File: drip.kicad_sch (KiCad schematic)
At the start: 37 parts, among them J1 ISP, Q1 2n2907, Q2 2n2907, Q3 2n2907, Q4 2n2907, Q5 2n2907, Q6 2n2907, Q7 2n2907, Q8 2n2907, SW1 8, SW10 Divide, SW11 Divide, SW12 Divide, SW2 5, SW3 2, SW4 Decimal, SW5 9, SW6 6, SW7 3, SW8 CHS, SW9 Divide, U1 74LS138, U2 5641AS-4Digit-7Segment, U3 5641AS-4Digit-7Segment, U4 MSP430G2553IN20

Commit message: Reducing pins
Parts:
- removed SW1: 8, Button_Switch_Keyboard:SW_Cherry_MX_1.00u_PCB, symbol Switch:SW_Push_45deg
- removed SW10, SW11, SW12, SW9: Divide, Button_Switch_Keyboard:SW_Cherry_MX_1.00u_PCB, symbol Switch:SW_Push_45deg
- removed SW2: 5, Button_Switch_Keyboard:SW_Cherry_MX_1.00u_PCB, symbol Switch:SW_Push_45deg
- removed SW3: 2, Button_Switch_Keyboard:SW_Cherry_MX_1.00u_PCB, symbol Switch:SW_Push_45deg
- removed SW4: Decimal, Button_Switch_Keyboard:SW_Cherry_MX_1.00u_PCB, symbol Switch:SW_Push_45deg
- removed SW5: 9, Button_Switch_Keyboard:SW_Cherry_MX_1.00u_PCB, symbol Switch:SW_Push_45deg
- removed SW6: 6, Button_Switch_Keyboard:SW_Cherry_MX_1.00u_PCB, symbol Switch:SW_Push_45deg
- removed SW7: 3, Button_Switch_Keyboard:SW_Cherry_MX_1.00u_PCB, symbol Switch:SW_Push_45deg
- removed SW8: CHS, Button_Switch_Keyboard:SW_Cherry_MX_1.00u_PCB, symbol Switch:SW_Push_45deg
- added JP? (x2): Jumper_2_Bridged, symbol Jumper:Jumper_2_Bridged
- added R? (x8): R_Small_US, symbol Device:R_Small_US
- added SW?: And, symbol Switch:SW_Push_45deg
- added SW?: 8, symbol Switch:SW_Push_45deg
- added SW?: 9, symbol Switch:SW_Push_45deg
- added SW?: Xor, symbol Switch:SW_Push_45deg
- added SW?: 2, symbol Switch:SW_Push_45deg
- added SW?: E, symbol Switch:SW_Push_45deg
- added SW?: Decimal, symbol Switch:SW_Push_45deg
- added SW?: Clear, symbol Switch:SW_Push_45deg
- added SW?: F, symbol Switch:SW_Push_45deg
- added SW?: 5, symbol Switch:SW_Push_45deg
- added SW?: A, symbol Switch:SW_Push_45deg
- added SW?: 1, symbol Switch:SW_Push_45deg
- added SW?: Shift, symbol Switch:SW_Push_45deg
- added SW?: 0, symbol Switch:SW_Push_45deg
- added SW?: K, symbol Switch:SW_Push_45deg
- added SW?: Dec, symbol Switch:SW_Push_45deg
- added SW?: Enter, symbol Switch:SW_Push_45deg
- added SW?: D, symbol Switch:SW_Push_45deg
- added SW?: 7, symbol Switch:SW_Push_45deg
- added SW?: Oct, symbol Switch:SW_Push_45deg
- added SW?: Mul, symbol Switch:SW_Push_45deg
- added SW?: Plus, symbol Switch:SW_Push_45deg
- added SW?: +/-, symbol Switch:SW_Push_45deg
- added SW?: Minus, symbol Switch:SW_Push_45deg
- added SW?: Or, symbol Switch:SW_Push_45deg
- added SW?: 3, symbol Switch:SW_Push_45deg
- added SW?: B, symbol Switch:SW_Push_45deg
- added SW?: Hex, symbol Switch:SW_Push_45deg
- added SW?: 1'sCompl, symbol Switch:SW_Push_45deg
- added SW?: 6, symbol Switch:SW_Push_45deg
- added SW?: Clear Entry, symbol Switch:SW_Push_45deg
- added SW?: Div, symbol Switch:SW_Push_45deg
- added SW?: Bin, symbol Switch:SW_Push_45deg
- added SW?: 4, symbol Switch:SW_Push_45deg
- added SW?: Store, symbol Switch:SW_Push_45deg
- added SW?: C, symbol Switch:SW_Push_45deg
- added SW?: Recall, symbol Switch:SW_Push_45deg
- added U?: 74LS595, Package_DIP:DIP-16_W7.62mm_Socket_LongPads, symbol 74xx:74LS595
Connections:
- net GND: now also JP?.1 (A), JP?.1 (A), U?.8 (GND)
- net VCC: now also U?.10 (~{SRCLR}), U?.16 (VCC)
- net ~{LED_SEL_0}: now also U4.2 (TA0CLK/ACLK/CA0/A0/P1.0)
- net ~{LED_SEL_1}: now also U4.3 (UCA0RXD/UCA0SOMI/TA0.0/CA1/A1/P1.1)
- net ~{LED_SEL_2}: now also U4.4 (UCA0TXD/UCA0SIMO/TA0.1/CA2/A2/P1.2)
- net d0: no longer names the net of U2.11 (A), U3.11 (A)
- net d0: now also R?.2; no longer U4.2 (TA0CLK/ACLK/CA0/A0/P1.0)
- net d1: no longer names the net of U2.7 (B), U3.7 (B)
- net d1: now also R?.2; no longer U4.3 (UCA0RXD/UCA0SOMI/TA0.0/CA1/A1/P1.1)
- net d2: no longer names the net of U2.4 (C), U3.4 (C)
- net d2: now also R?.2; no longer U4.4 (UCA0TXD/UCA0SIMO/TA0.1/CA2/A2/P1.2)
- net d3: no longer names the net of U2.2 (D), U3.2 (D)
- net d3: now also R?.2; no longer U4.5 (CAOUT/VREF-/VeREF-/CA3/A3/P1.3)
- net d4: no longer names the net of U2.1 (E), U3.1 (E)
- net d4: now also R?.2; no longer U4.6 (TCK/SMCLK/UCB0STE/UCA0CLK/VREF+/VeREF+/CA4/A4/P1.4)
- net d5: no longer names the net of U2.10 (F), U3.10 (F)
- net d5: now also R?.2; no longer U4.7 (TMS/UCB0CLK/UCA0STE/TA0.0/CA5/A5/P1.5)
- net d6: no longer names the net of U2.5 (G), U3.5 (G)
- net d6: now also R?.2; no longer U4.14 (TDI/TCLK/UCB0SOMI/UCB0SCL/TA0.1/CA6/A6/P1.6)
- net d7: no longer names the net of U2.3 (DP), U3.3 (DP)
- net d7: now also R?.2; no longer U4.15 (TDO/TDI/UCB0SIMO/UCB0SDA/CAOUT/CA7/A7/P1.7)
- new net: JP?.2 (B), U?.13 (~{OE})
- new net: JP?.2 (B), U?.12 (RCLK)
- new net LED_A: R?.1, U?.15 (QA)
- new net LED_B: R?.1, U?.1 (QB)
- new net LED_C: R?.1, U?.2 (QC)
- new net LED_CLOCK: U4.6 (TCK/SMCLK/UCB0STE/UCA0CLK/VREF+/VeREF+/CA4/A4/P1.4), U?.11 (SRCLK)
- new net LED_D: R?.1, U?.3 (QD)
- new net LED_DATA: U4.5 (CAOUT/VREF-/VeREF-/CA3/A3/P1.3), U?.14 (SER)
- new net LED_DP: R?.1, U?.7 (QH)
- new net LED_E: R?.1, U?.4 (QE)
- new net LED_F: R?.1, U?.5 (QF)
- new net LED_G: R?.1, U?.6 (QG)
- no-connect marks 0 -> 1
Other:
- note added: "4.7kΩ or more seems like the ticket here (< 1mA)"
- note removed: "TODO: Do I really need an 8-bit data?"

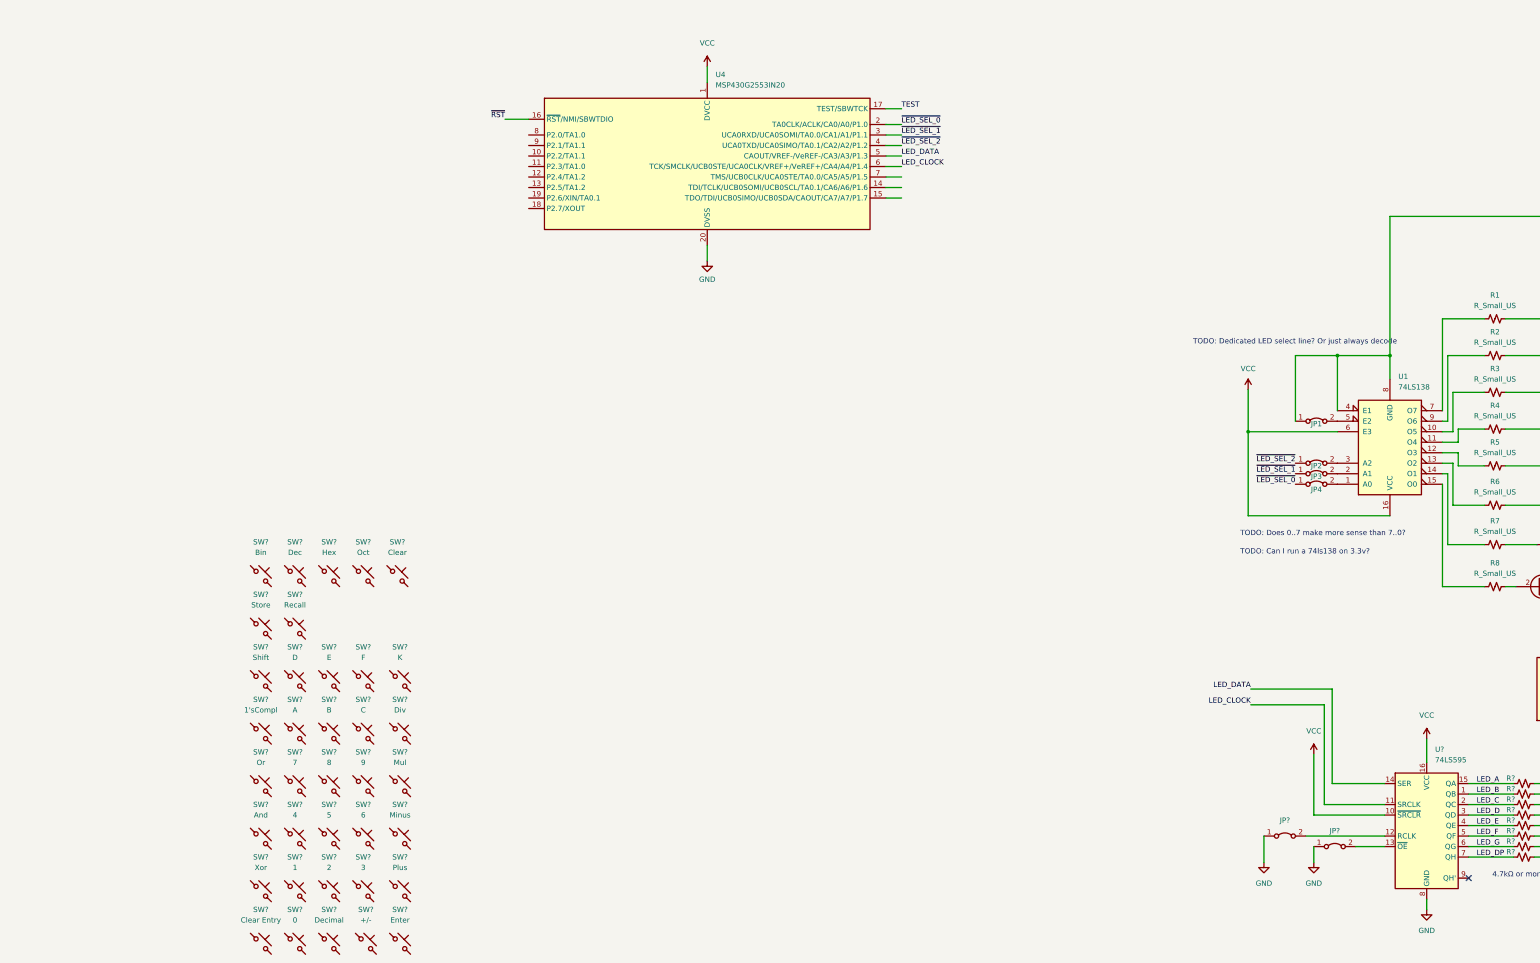
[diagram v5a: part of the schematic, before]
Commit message: Keyboard row decode
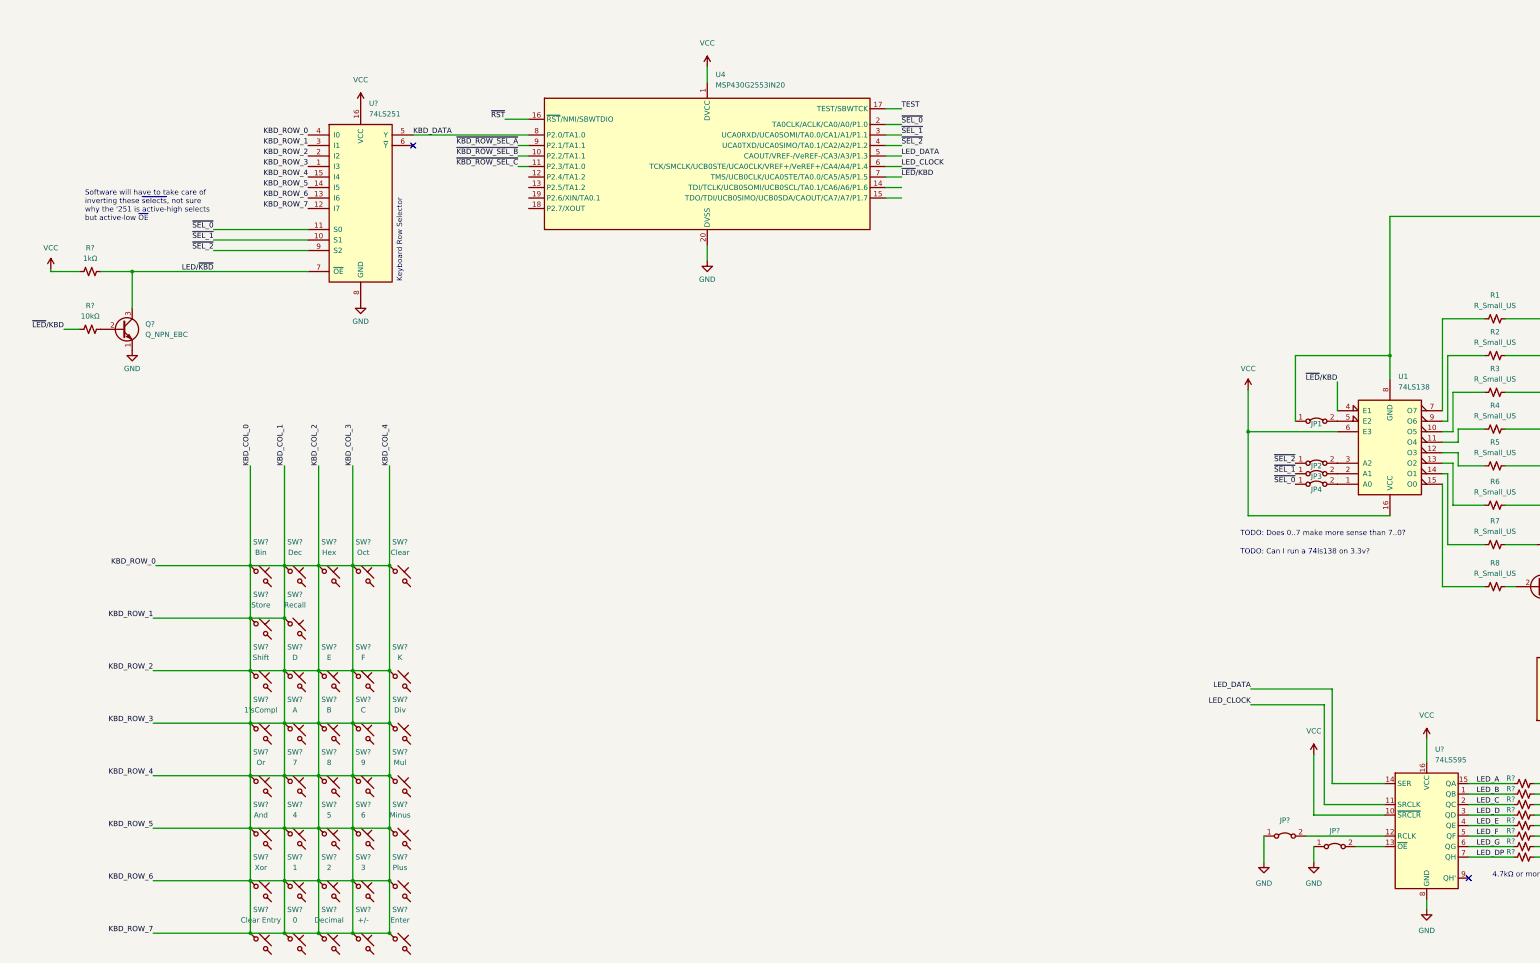
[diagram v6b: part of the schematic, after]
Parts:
- added Q?: Q_NPN_EBC, symbol Device:Q_NPN_EBC
- added R?: 1kΩ, symbol Device:R_Small_US
- added R?: 10kΩ, symbol Device:R_Small_US
- added U?: 74LS251, symbol 74xx:74LS251
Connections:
- net GND: now also Q?.1 (E), U?.8 (GND); no longer U1.4 (E1)
- net VCC: now also R?.1, U?.16 (VCC)
- net KBD_COL_0: now reaches SW?.1
- net KBD_COL_0: now also SW?.1, SW?.1, SW?.1, SW?.1, SW?.1, SW?.1, SW?.1, SW?.1, SW?.1, SW?.1, SW?.1, SW?.1, SW?.1, SW?.1, SW?.1, SW?.1, SW?.1, SW?.1, SW?.1, SW?.1, SW?.1, SW?.1, SW?.1, SW?.1, SW?.1, SW?.1, SW?.1, SW?.1, SW?.1, SW?.1, SW?.1, SW?.1, SW?.1, SW?.1, SW?.1, SW?.1, U?.1 (I3), U?.12 (I7), U?.13 (I6), U?.14 (I5), U?.15 (I4), U?.2 (I2), U?.3 (I1), U?.4 (I0)
- net ~{KBD_ROW_SEL_B}: now reaches U4.10 (P2.2/TA1.1)
- net ~{KBD_ROW_SEL_C}: now reaches U4.11 (P2.3/TA1.0)
- net ~{LED}/KBD: now reaches U4.7 (TMS/UCB0CLK/UCA0STE/TA0.0/CA5/A5/P1.5)
- net ~{LED}/KBD: now also U1.4 (E1), R?.1
- net KBD_DATA: now reaches U4.8 (P2.0/TA1.0)
- net KBD_DATA: now also U?.5 (Y)
- net ~{KBD_ROW_SEL_A}: now reaches U4.9 (P2.1/TA1.1)
- net ~{LED_SEL_0} renamed ~{SEL_0}
- net ~{SEL_0}: now also U?.11 (S0)
- net ~{LED_SEL_1} renamed ~{SEL_1}
- net ~{SEL_1}: now also U?.10 (S1)
- net ~{LED_SEL_2} renamed ~{SEL_2}
- net ~{SEL_2}: now also U?.9 (S2)
- new net: Q?.2 (B), R?.2
- new net LED/~{KBD}: Q?.3 (C), R?.2, U?.7 (~{OE})
- no-connect marks 1 -> 2
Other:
- note added: "Keyboard Row Selector"
- note added: "Software will have to take care of inverting these ~{selects}, not sure why the '251 is active-high selects but active-low ~{OE}"
- note removed: "TODO: Dedicated LED select line? Or just always decode"
- moved on the sheet: SW?

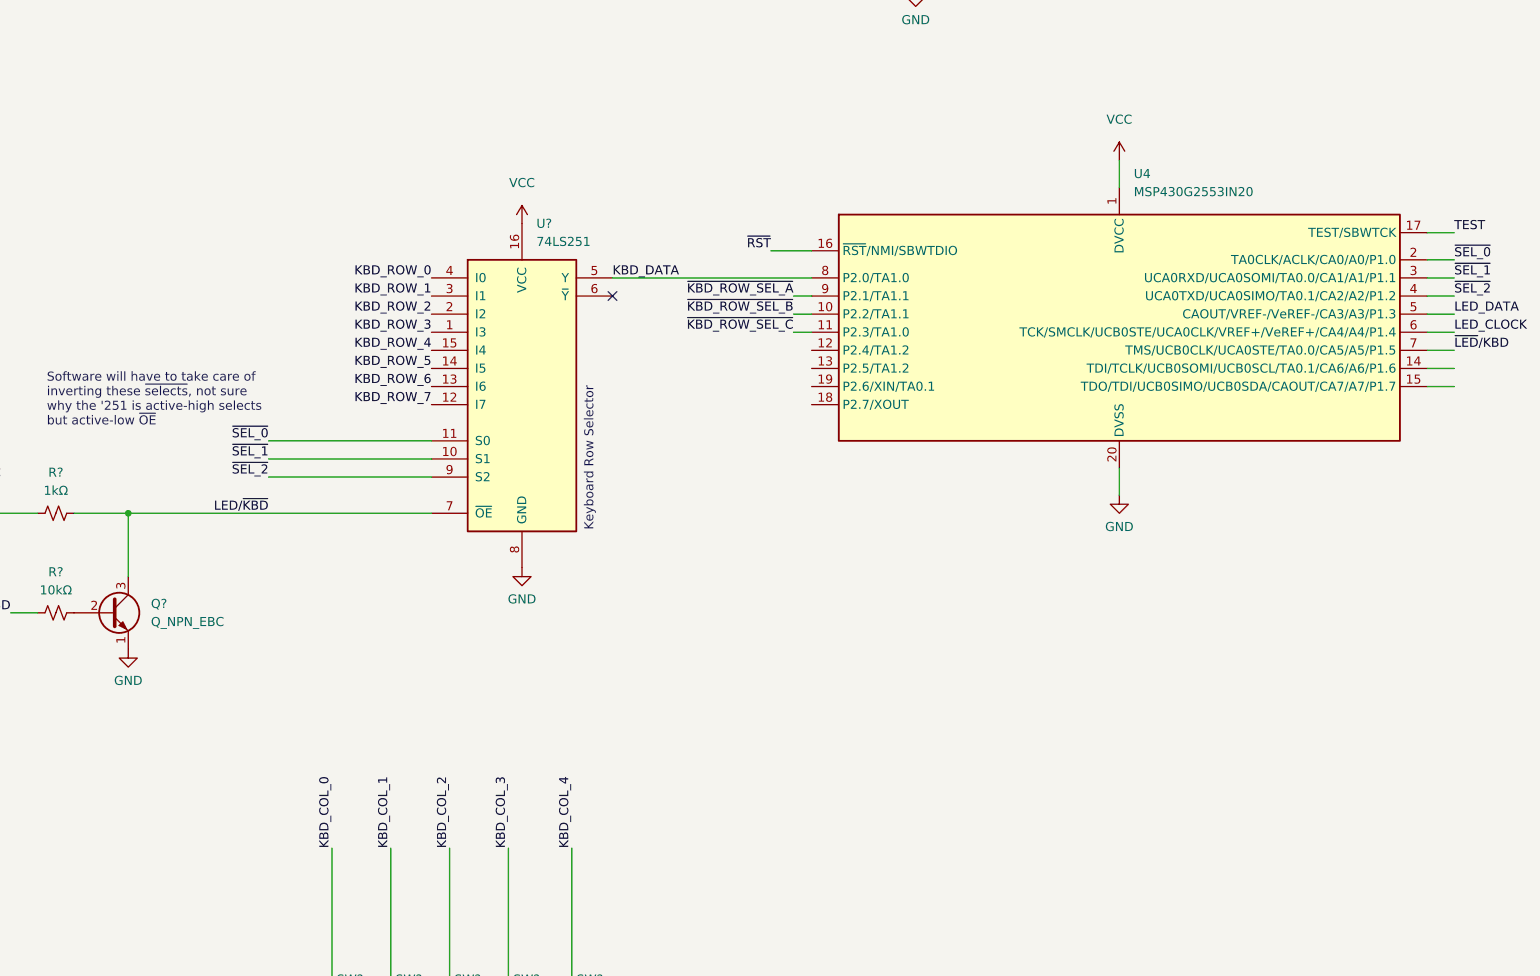
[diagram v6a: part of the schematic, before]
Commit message: Keyboard column decode
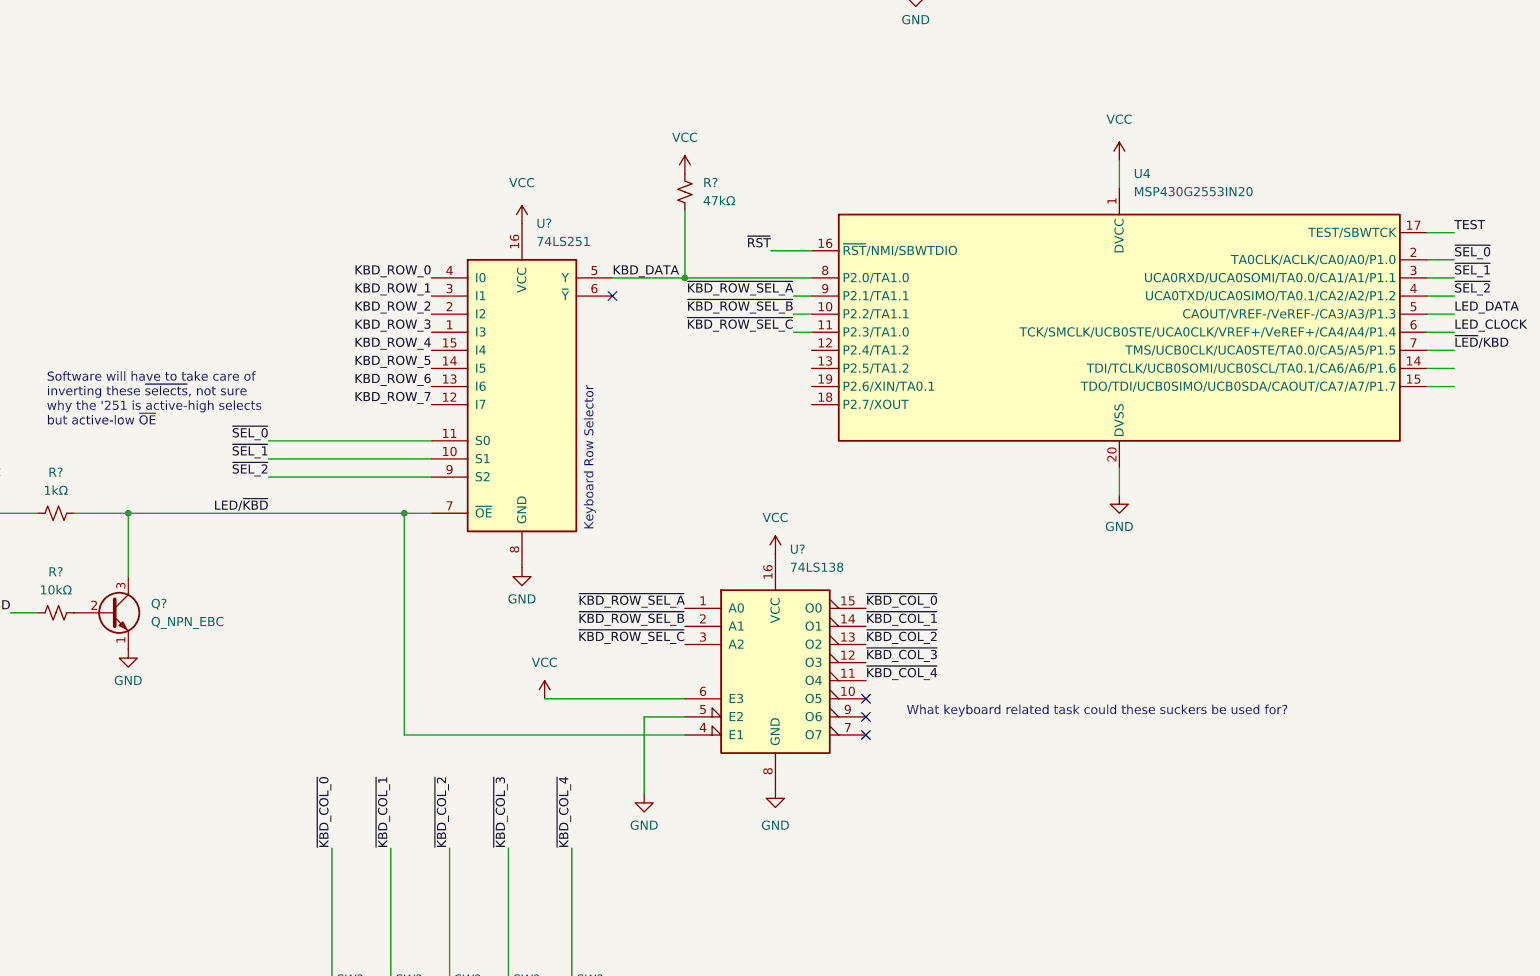
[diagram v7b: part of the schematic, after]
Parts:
- added R?: 47kΩ, symbol Device:R_Small_US
- added U?: 74LS138, symbol 74xx:74LS138
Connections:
- net GND: now also U?.5 (E2), U?.8 (GND)
- net KBD_DATA: now also R?.2
- net LED/~{KBD}: now also U?.4 (E1)
- net VCC: now also R?.1, U?.16 (VCC), U?.6 (E3)
- net ~{KBD_ROW_SEL_A}: now also U?.1 (A0)
- net ~{KBD_ROW_SEL_B}: now also U?.2 (A1)
- net ~{KBD_ROW_SEL_C}: now also U?.3 (A2)
- net KBD_COL_0 renamed KBD_ROW_0
- net KBD_ROW_0: now also U?.11 (O4), U?.12 (O3), U?.13 (O2), U?.14 (O1), U?.15 (O0)
- no-connect marks 2 -> 5
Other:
- note added: "What keyboard related task could these suckers be used for?"
